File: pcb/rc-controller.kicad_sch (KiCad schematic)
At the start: 73 parts, among them J1 USB_C_Receptacle_USB2.0, M1 Motor_DC, Q1 AO3401A, Q2 AO3401A, Q3 AO3400A, Q4 AO3400A, SW1 SW_SPDT, SW2 SW_SPDT, SW3 SW_DPST, SW4 SW_DPST, SW5 SW_DPST, SW6 SW_DPST, U1 STM32F401RCTx, U2 LPS22HB, U3 SRV05-4, U4 TX4401, U5 ICM-42670-P, U6 TP4057-42, U7 nrf24L01P_PA_LNA, U8 SSD1306

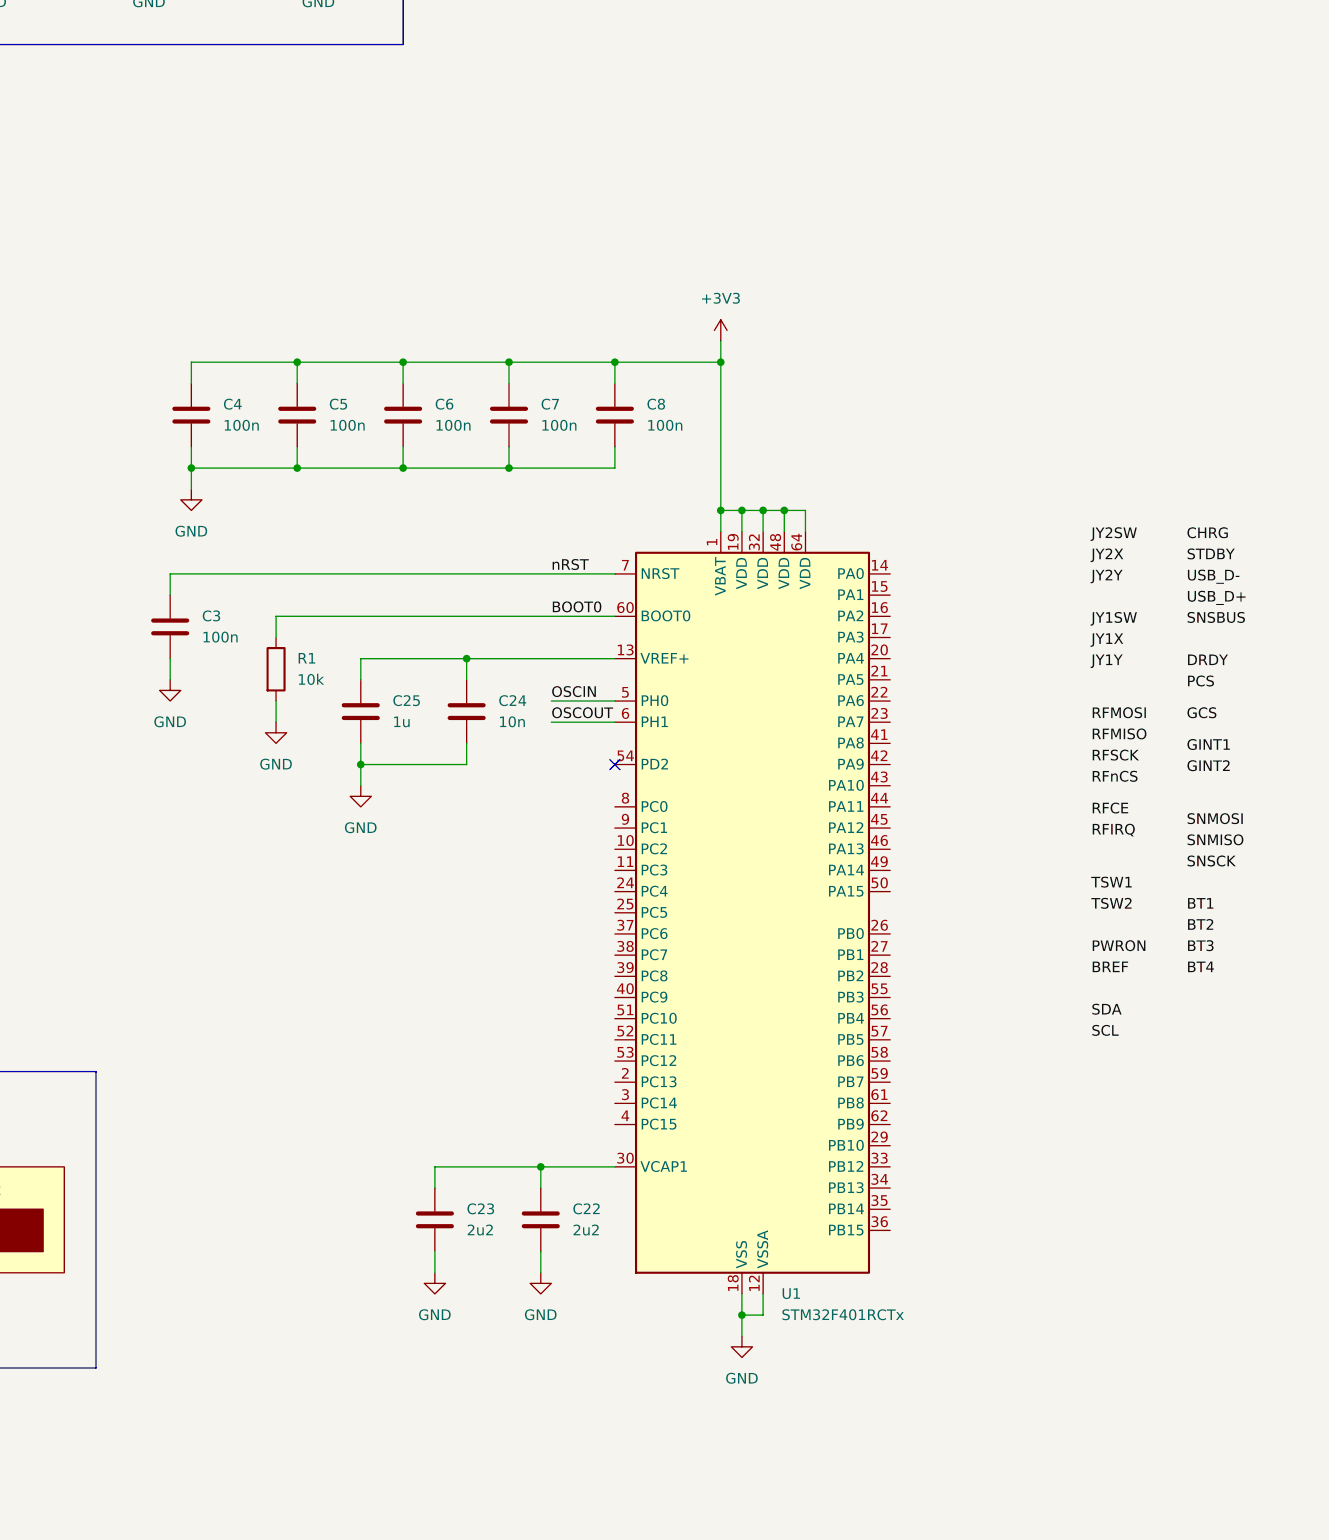
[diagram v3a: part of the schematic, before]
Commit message: Add crystal oscillator
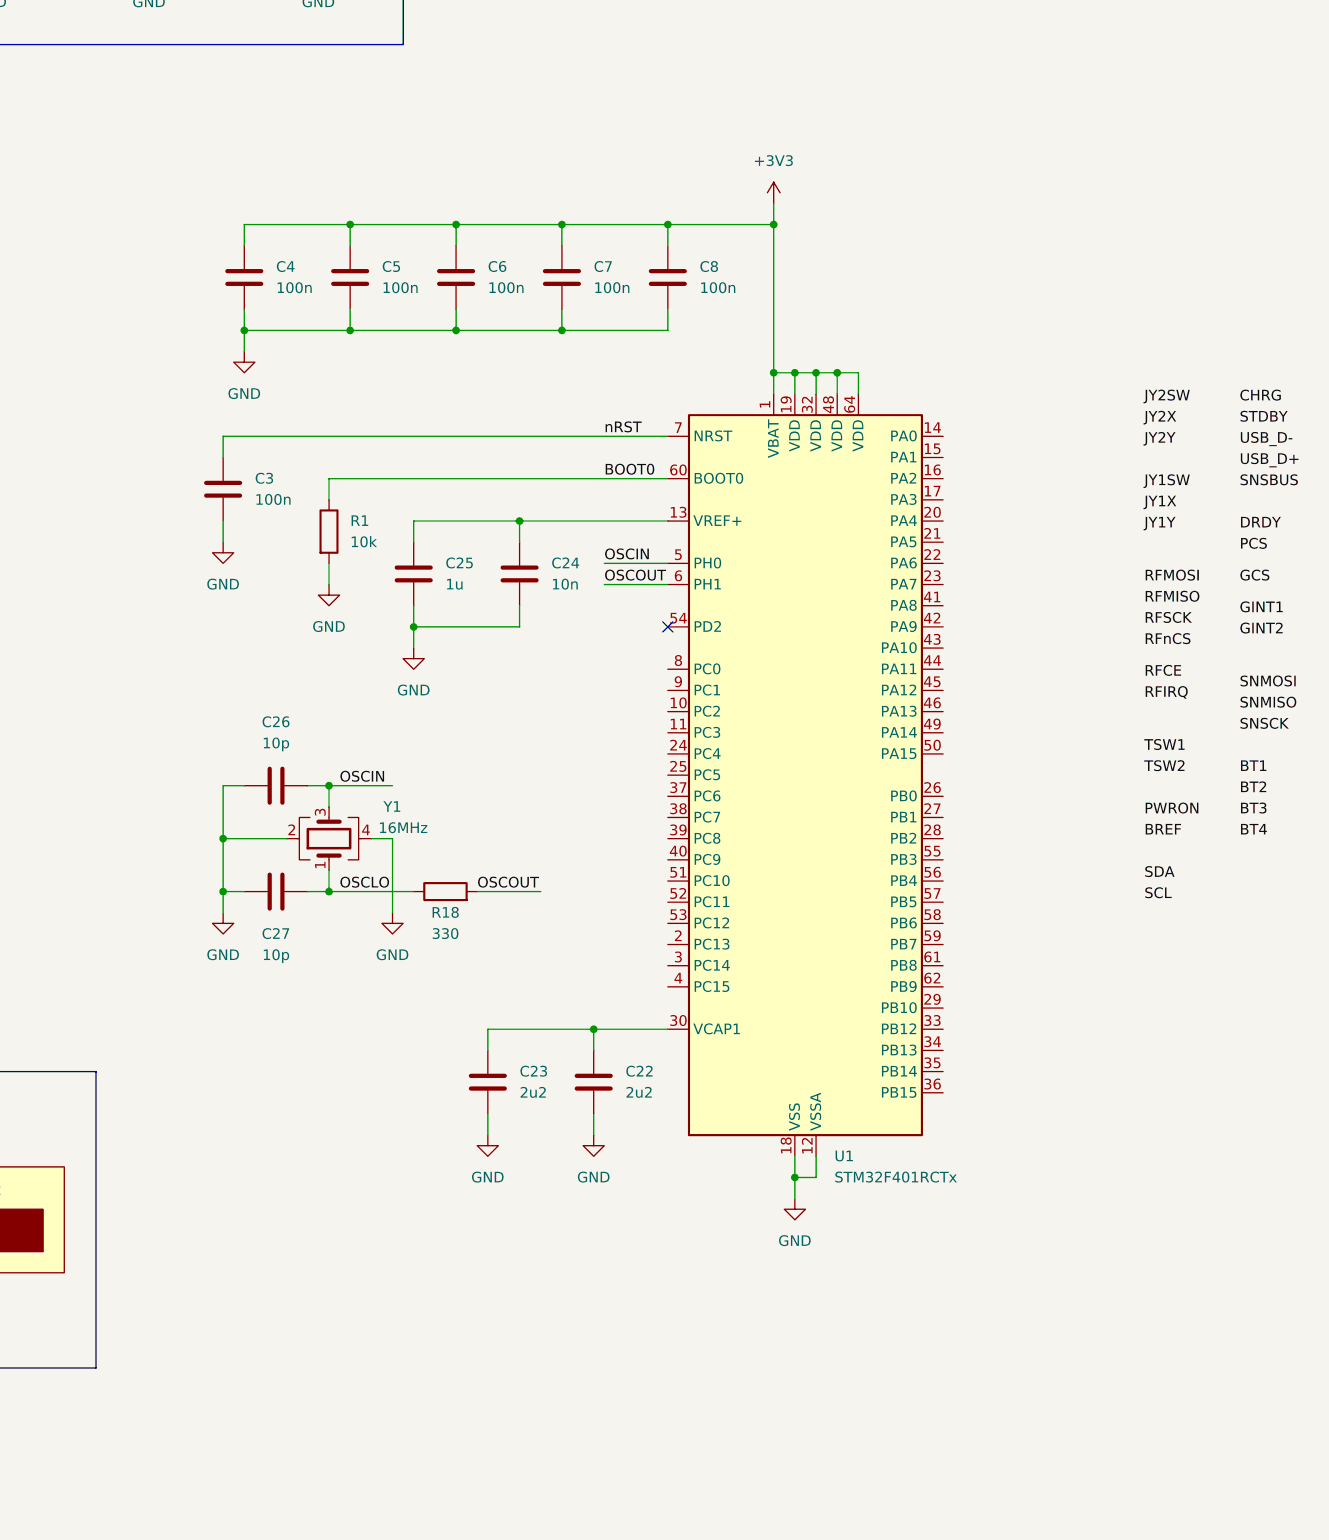
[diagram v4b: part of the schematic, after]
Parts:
- added C26, C27: 10p, Capacitor_SMD:C_0402_1005Metric, symbol Device:C
- added R18: 330, Resistor_SMD:R_0402_1005Metric, symbol Device:R
- added Y1: 16MHz, Crystal:Crystal_SMD_3225-4Pin_3.2x2.5mm, symbol Device:Crystal_GND24
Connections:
- net GND: now also C26.1, C27.1, Y1.2, Y1.4
- net OSCIN: now also C26.2, Y1.3
- net OSCOUT: now also R18.2
- new net OSCLO: C27.2, R18.1, Y1.1
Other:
- moved on the sheet: C22, C23, C24, C25, C3, C4, C5, C6, C7, C8, R1, U1

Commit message: Configure USB
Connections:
- net SNSBUS: now also U1.42 (PA9)
- net USB_D+: now also U1.45 (PA12)
- net USB_D-: now also U1.44 (PA11)
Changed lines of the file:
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@@
 	(wire
 		(pts
+			(xy 382.27 140.97) (xy 391.16 140.97)
+		)
+		(stroke
+			(width 0)
+			(type default)
+		)
+	)
+	(wire
+		(pts
 			(xy 114.3 69.85) (xy 116.84 69.85)
 		)
@@
 	(wire
 		(pts
+			(xy 382.27 133.35) (xy 391.16 133.35)
+		)
+		(stroke
+			(width 0)
+			(type default)
+		)
+	)
+	(wire
+		(pts
 			(xy 284.48 45.72) (xy 289.56 45.72)
 		)
@@
 		)
 	)
+	(wire
+		(pts
+			(xy 382.27 138.43) (xy 391.16 138.43)
+		)
+		(stroke
+			(width 0)
+			(type default)
+		)
+	)
 	(polyline
 		(pts
@@
 	)
 	(label "USB_D+"
-		(at 417.83 114.3 0)
+		(at 383.54 140.97 0)
 		(fields_autoplaced yes)
 		(effects
@@
 	)
 	(label "SNSBUS"
-		(at 417.83 116.84 0)
+		(at 383.54 133.35 0)
 		(fields_autoplaced yes)
 		(effects
@@
 	)
 	(label "USB_D-"
-		(at 417.83 111.76 0)
+		(at 383.54 138.43 0)
 		(fields_autoplaced yes)
 		(effects
